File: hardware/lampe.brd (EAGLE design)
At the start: 63.2 x 62.2 mm, 45 parts, among them IC1 LM393N, IC2 ATMEGA168-20P, IC3 DS1307, Q1 IRFU9024N, Q2 16MHz, Q3 32.768kHz, T1 BC457B, T2 BC557B, T3 BC457B

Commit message: Cleanup
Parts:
- removed C2: 100nF, rcl:C025-025X050
- removed C3: 100uF, rcl:E2,5-6E
- removed C4: 22pF, rcl:C025-025X050
- removed C5: 100nF, rcl:C050-025X075
- removed D1: 1N4148, diode:D-2.5
- removed D2: 1N4148, diode:DO35-10
- removed D3: SB140, diode:ZDIO-2.5
- removed IC2: ATMEGA168-20P, adafruit:DIL28-3
- removed JP2: SUPPLY, pinhead:1X02
- removed JP3: (no value), pinhead:1X04
- removed L1: 100uH, rcl:6000-XXXX-RC
- removed Q1: IRFU9024N, transistor-power:I-PAK_TO251AA
- removed R1, R5: 10k, rcl:0204/5
- removed R10, R3: 4.7k, rcl:0204V
- removed R14: 10k, rcl:0204V
- removed R15: 15k, rcl:0207/10
- removed R2: 10k, rcl:RTRIM64W
- removed R22, R8: 1R*, rcl:0204/7
- removed R23: 4.7k, rcl:0204/7
- removed R4: 1k, rcl:0204/5
- removed R6: 10k, rcl:0207/10
- removed R7: 10R, rcl:0204/5
- removed R9: 1k, rcl:0207/10
- removed T1: BC457B, transistor:TO92-EBC
- removed T2: BC557B, transistor:TO92-EBC
- added ISP1: AVRISP-6, adafruit:AVRISP
- added KK1: PF750, heatsink:PF752
- added Q4: BUZ11BV, transistor-power:TO220BV
- added R24: 10, rcl:0204/7
- added R25, R30: 1W, rcl:0411/12
- added R26: 560, rcl:0204/7
- added R27: 10k, rcl:0207/10
- added R28: 10k, rcl:0204/5
- added R29: 1k, rcl:0204V
- added T4: BC547B, transistor-neu-to92:TO92-EBC
- added X1, X2: MKDSN1,5/2-5,08, con-phoenix-508:MKDSN1,5/2-5,08
- C1: value 1uF -> 100nF; device rcl:E2,5-6E -> rcl:C050-025X075
- C10: value 10uF -> 100pF; device rcl:E2,5-6E -> rcl:C025-025X050
- IC1: value LM393N -> ATMEGA168-20P; device linear:DIL08 -> adafruit:DIL28-3
- JP1: value LED -> GPIO; device pinhead:1X02 -> pinhead:1X05
- Q2: value 16MHz -> 16Mhz; device crystal:HC49/S -> adafruit:HC18U-V
- R11: device rcl:0204V -> rcl:0207/10
- T3: value BC457B -> BC547B; device transistor:TO92-EBC -> transistor-neu-to92:TO92-EBC
- moved JP1 47.1 mm to (40.6, 31.8), turned to 90 degrees
- moved IC1 33.2 mm to (49.5, 45.7), turned to 270 degrees
- moved C1 27.9 mm to (63.5, 49.5), turned to 180 degrees
- moved G1 17.8 mm to (81.3, 67.3), turned to 270 degrees
- moved C8 17.6 mm to (55.9, 45.7), turned to 90 degrees
- moved IC3 13.5 mm to (64.8, 63.5)
- moved Q3 13.5 mm to (67.3, 69.8)
- moved Q2 11.7 mm to (35.6, 41.9)
- moved R13 10.2 mm to (55.9, 63.5)
- moved C6 10.2 mm to (43.2, 41.9)
- moved R12 10.2 mm to (58.4, 62.2)
- moved C9 8.52 mm to (41.9, 47.0), turned to 180 degrees
- moved C7 8.13 mm to (40.6, 43.2), turned to 90 degrees
- moved C10 7.73 mm to (64.8, 36.8)
- moved T3 6.35 mm to (63.5, 40.6), turned to 0 degrees
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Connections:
- removed net N$10: IC1.7, R10.2, T1.B, T2.B
- removed net N$11: R7.1, T1.E, T2.E
- removed net N$15: D3.C, L1.2, Q1.2
- removed net N$16: Q1.1, R7.2
- removed net N$17: JP1.1, L1.1
- removed net N$20: IC2.1, R11.2
- removed net N$25: IC2.17, R15.2
- removed net N$26: C10.+, R14.1, R15.1, T3.B
- removed net N$27: IC2.5, JP3.2
- removed net N$28: IC2.6, JP3.3
- removed net N$30: C7.1, IC2.9, Q2.2
- new net N$37: Q4.G, R24.2
- new net N$38: Q4.D, X2.2
- new net N$39: Q4.S, R25.2, R26.1, R30.2
- new net N$40: C10.1, R26.2, T3.B
- new net N$41: C1.1, C10.2, R27.2, R28.2, T3.C, T4.B
- new net N$43: R24.1, R29.2, T4.E
- net +5V: now also IC1.20, IC1.21, IC1.7, ISP1.2, T4.C, X1.2, X2.1; no longer C2.1, C3.+, C5.1, IC1.8, IC2.20, IC2.21, IC2.7, JP2.2, Q1.3, R10.1, R23.1, R3.1, R5.1, T1.C
- net GND: now also C1.2, IC1.22, IC1.8, ISP1.6, JP1.1, R25.1, R28.1, R29.1, R30.1, X1.1; no longer C1.-, C10.-, C2.2, C3.-, C4.2, C5.2, D1.C, D3.A, IC1.4, IC2.22, IC2.8, JP2.1, JP3.4, R14.2, R22.2, R4.2, R6.2, R8.2, T2.C
- net N$1: now also IC1.15, R27.1; no longer D1.A, R1.1, R3.2
- net N$12: now also C7.1, IC1.9, Q2.2; no longer IC2.3, U$1.RXD
- net N$18: now also IC1.10; no longer IC2.10
- net N$19: now also IC1.28; no longer IC2.28
- net N$2: now also IC1.18, ISP1.1; no longer R1.2, R2.3
- net N$21: now also IC1.27; no longer IC2.27
- net N$23: now also IC1.3; no longer IC2.2
- net N$24: now also IC1.2, U$1.RXD; no longer IC2.4, JP3.1
- net N$3: now also IC1.19, ISP1.3; no longer C1.+, IC1.2, R2.2
- net N$4: now also IC1.1, ISP1.5, R11.2; no longer R2.1, R4.1
- net N$5: now also IC1.17, ISP1.4; no longer JP1.2, R22.1, R8.1, R9.2
- net N$6: now also IC1.12, JP1.4; no longer C4.1, IC1.3, R9.1
- net N$7: now also IC1.11, JP1.5; no longer D2.C, IC1.1
- net N$8: now also IC1.13, JP1.3; no longer D2.A, IC1.5, R23.2
- net N$9: now also IC1.14, JP1.2; no longer IC1.6, R5.2, R6.1, T3.C
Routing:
- net +5V: track 229.9 -> 140.2 mm
- net N$4: track 2.54 -> 43.2 mm
- net GND: track 336.6 -> 298.5 mm
- net N$9: track 40.6 -> 5.08 mm, vias 2 -> 0
- net N$10: track 27.9 -> 0.00 mm
- net N$39: track 0.00 -> 26.7 mm
- net N$37: track 0.00 -> 25.4 mm
- net N$41: track 0.00 -> 25.4 mm
- net N$5: track 7.62 -> 31.8 mm, vias 0 -> 2
- net N$38: track 0.00 -> 22.8 mm
- net N$2: track 5.08 -> 25.4 mm
- net N$30: track 15.5 -> 0.00 mm
- net N$26: track 15.2 -> 0.00 mm
- net N$11: track 15.2 -> 0.00 mm
- net N$21: track 20.3 -> 7.62 mm
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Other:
- board size 63.2 x 62.2 mm -> 68.2 x 68.6 mm
- board text added: "Lampe rev. 1"

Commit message: Minors.
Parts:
- added R1: 1k, rcl:0204V
- added R2: 10k, ptc-ntc:B57164
- R27: value 10k -> 6.1k
- R28: value 10k -> 1k
- R29: value 1k -> 10k
- moved ISP1 2.54 mm to (50.8, 22.9)
- moved R27 2.54 mm to (61.0, 29.2)
- moved U$1 2.54 mm to (38.1, 55.9)
- moved X1 2.54 mm to (73.7, 21.6)
- moved X2 2.54 mm to (83.8, 21.6)
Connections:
- new net N$10: IC1.23, R1.1, R2.1
- net +5V: now also R2.2
- net GND: now also R1.2
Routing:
- net +5V: track 140.2 -> 147.8 mm
- net GND: track 298.5 -> 306.1 mm
- net N$10: track 0.00 -> 5.08 mm
- net N$3: track 15.2 -> 17.8 mm
- net N$2: track 25.4 -> 27.9 mm
- net N$41: track 25.4 -> 27.9 mm
- net N$4: track 43.2 -> 45.7 mm
- net N$24: track 5.08 -> 7.62 mm
- net N$23: track 5.08 -> 7.62 mm
- net N$1: track 5.08 -> 2.54 mm
- net N$5: track 31.8 -> 34.3 mm
- net N$38: track 22.8 -> 25.4 mm
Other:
- board text added: "G"
- board text added: "R"
- board text added: "T"
- board text added: "V"

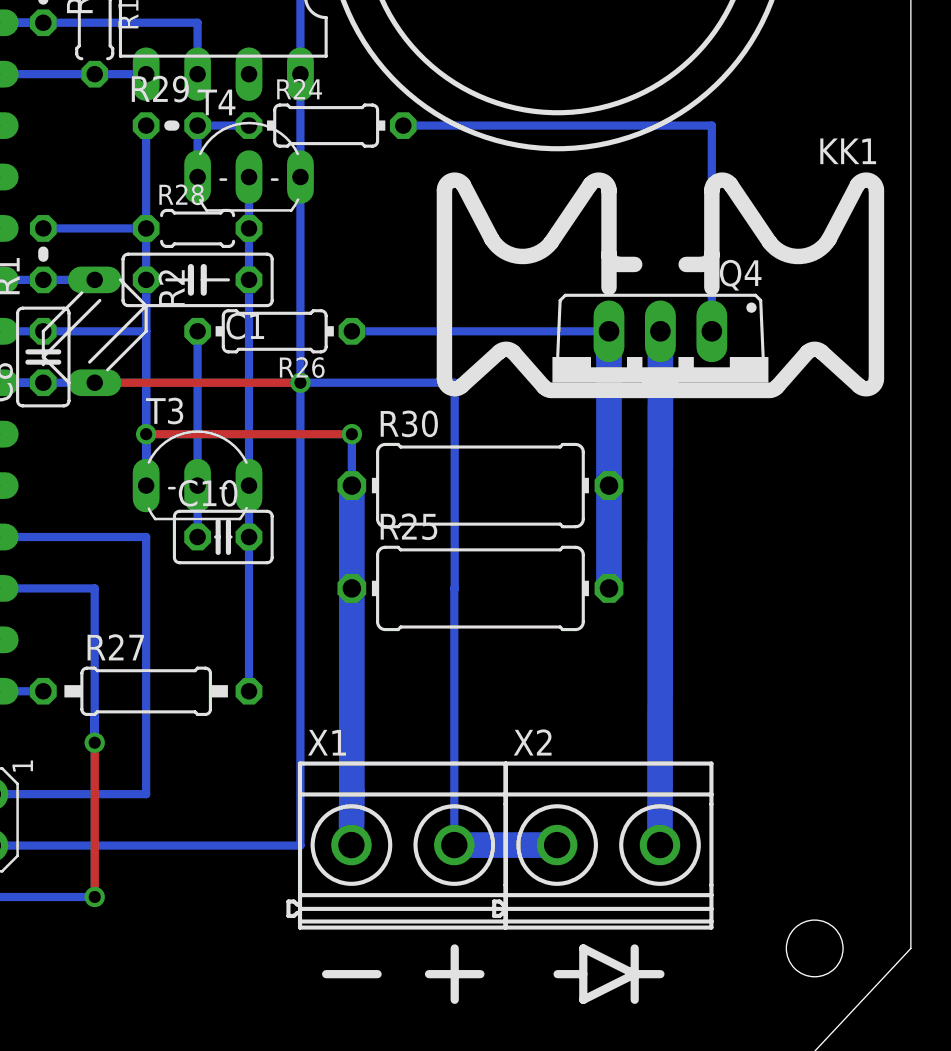
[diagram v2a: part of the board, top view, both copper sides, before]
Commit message: Fixed current reg.
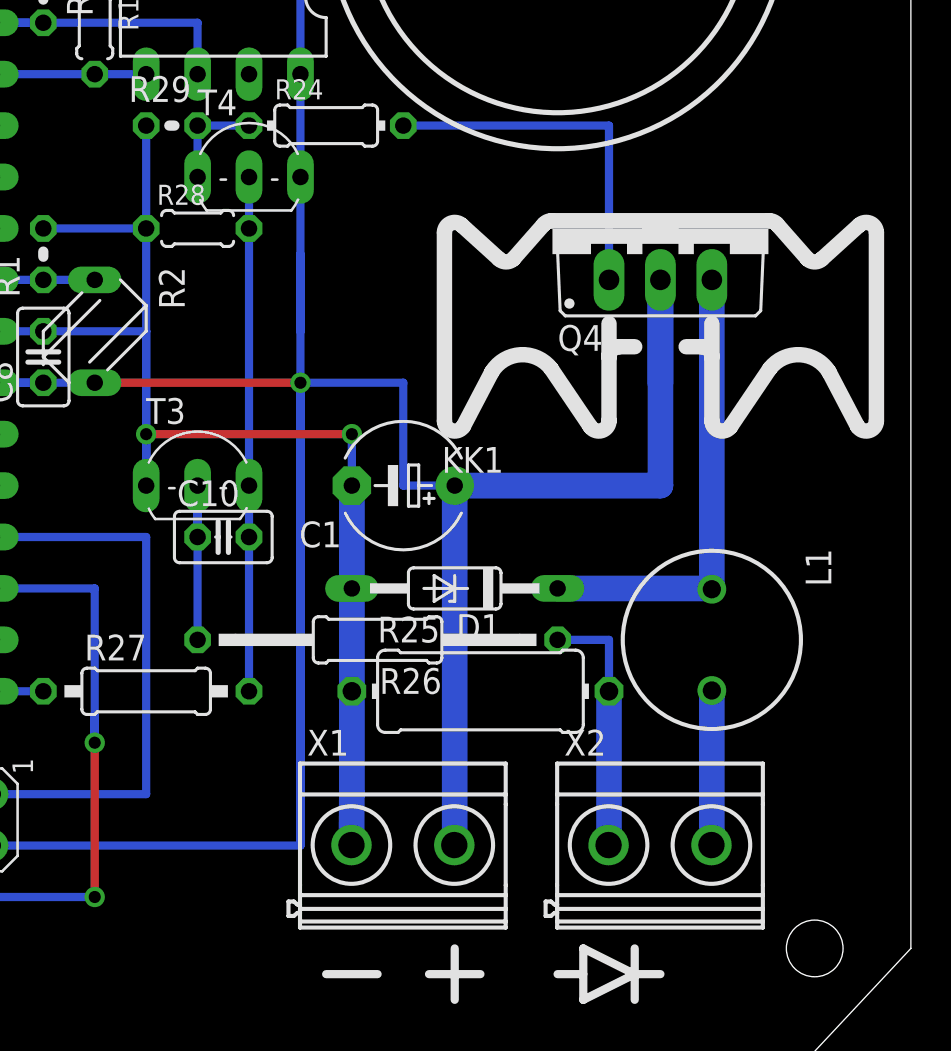
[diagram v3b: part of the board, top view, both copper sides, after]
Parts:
- removed R30: 1W, rcl:0411/12
- added D1: SB140, diode:DO35Z10
- added L1: 100uH, rcl:6000-XXXX-RC
- C1: value 100nF -> 100uF/35V; device rcl:C050-025X075 -> rcl:E5-6
- R26: device rcl:0204/7 -> rcl:0207/17
- R27: value 6.1k -> 4.7k
- moved R26 16.1 mm to (72.4, 31.8)
- moved C1 14.4 mm to (73.7, 39.4)
- moved KK1 7.62 mm to (86.4, 52.1), turned to 0 degrees
- moved Q4 7.62 mm to (86.4, 52.1), turned to 0 degrees
- moved R25 5.08 mm to (77.5, 29.2)
- moved X2 2.54 mm to (86.4, 21.6)
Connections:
- removed net N$38: Q4.D, X2.2
- new net N$11: D1.C, L1.1, Q4.S
- new net N$15: L1.2, X2.2
- net +5V: now also C1.+, Q4.D; no longer X2.1
- net GND: now also C1.-, D1.A; no longer C1.2, R30.1
- net N$39: now also X2.1; no longer Q4.S, R30.2
- net N$41: no longer C1.1
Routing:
- net +5V: track 147.8 -> 198.6 mm
- net N$38: track 25.4 -> 0.00 mm
- net N$11: track 0.00 -> 22.9 mm
- net N$39: track 26.7 -> 12.7 mm
- net N$15: track 0.00 -> 7.66 mm
- net N$37: track 25.4 -> 17.8 mm
- net GND: track 306.1 -> 303.6 mm
- net N$41: track 27.9 -> 25.4 mm

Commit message: Updated circuit and board PDFs.
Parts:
- moved T4 5.08 mm to (66.0, 50.8)
- moved R24 5.08 mm to (69.8, 52.1)
- moved R28 5.08 mm to (63.5, 47.0)
- moved R29 5.08 mm to (62.2, 52.1)
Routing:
- net GND: track 303.6 -> 223.5 mm
- net +5V: track 198.6 -> 165.5 mm
- net N$41: track 25.4 -> 20.3 mm
- net N$37: track 17.8 -> 12.7 mm
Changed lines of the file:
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@@
 <?xml version="1.0" encoding="utf-8"?>
 <!DOCTYPE eagle SYSTEM "eagle.dtd">
-<eagle version="7.1.0">
+<eagle version="7.2.0">
 <drawing>
 <settings>
@@
 <element name="R13" library="rcl" package="0204V" value="10k" x="55.88" y="63.5" rot="R270"/>
 <element name="U$1" library="jy-mcu" package="JY-MCU" value="JY-MCU" x="38.1" y="55.88" rot="R180"/>
-<element name="R24" library="rcl" package="0204/7" value="10" x="69.85" y="57.15"/>
+<element name="R24" library="rcl" package="0204/7" value="10" x="69.85" y="52.07"/>
 <element name="Q4" library="transistor-power" package="TO220BV" value="BUZ11BV" x="86.36" y="52.07"/>
 <element name="R25" library="rcl" package="0411/12" value="1W" x="77.47" y="29.21"/>
@@
 <element name="C10" library="rcl" package="C025-025X050" value="100pF" x="64.77" y="36.83"/>
 <element name="R27" library="rcl" package="0207/10" value="4.7k" x="60.96" y="29.21"/>
-<element name="R28" library="rcl" package="0204/5" value="1k" x="63.5" y="52.07"/>
-<element name="T4" library="transistor-neu-to92" package="TO92-EBC" value="BC547B" x="66.04" y="55.88"/>
-<element name="R29" library="rcl" package="0204V" value="10k" x="62.23" y="57.15"/>
+<element name="R28" library="rcl" package="0204/5" value="1k" x="63.5" y="46.99"/>
+<element name="T4" library="transistor-neu-to92" package="TO92-EBC" value="BC547B" x="66.04" y="50.8"/>
+<element name="R29" library="rcl" package="0204V" value="10k" x="62.23" y="52.07"/>
 <element name="X1" library="con-phoenix-508" package="MKDSN1,5/2-5,08" value="MKDSN1,5/2-5,08" x="73.66" y="21.59"/>
 <element name="X2" library="con-phoenix-508" package="MKDSN1,5/2-5,08" value="MKDSN1,5/2-5,08" x="86.36" y="21.59"/>
@@
 <contactref element="R12" pad="1"/>
 <wire x1="68.58" y1="59.69" x2="68.58" y2="64.77" width="0.4064" layer="16"/>
-<wire x1="59.69" y1="64.77" x2="58.42" y2="64.77" width="0.4064" layer="16"/>
 <contactref element="C9" pad="1"/>
 <contactref element="U$1" pad="VCC"/>
 <contactref element="T4" pad="C"/>
-<wire x1="68.58" y1="54.61" x2="68.58" y2="59.69" width="0.4064" layer="16"/>
+<wire x1="68.58" y1="49.53" x2="68.58" y2="59.69" width="0.4064" layer="16"/>
 <wire x1="38.1" y1="52.07" x2="43.18" y2="52.07" width="0.4064" layer="16"/>
-<wire x1="68.58" y1="64.77" x2="59.69" y2="64.77" width="0.4064" layer="16"/>
-<wire x1="68.58" y1="54.61" x2="68.58" y2="46.99" width="0.4064" layer="16"/>
+<wire x1="68.58" y1="64.77" x2="58.42" y2="64.77" width="0.4064" layer="16"/>
 <contactref element="ISP1" pad="2"/>
 <contactref element="IC1" pad="7"/>
@@
 <contactref element="X1" pad="2"/>
 <wire x1="53.34" y1="21.59" x2="68.58" y2="21.59" width="0.4064" layer="16"/>
-<wire x1="68.58" y1="21.59" x2="68.58" y2="44.45" width="0.4064" layer="16"/>
 <via x="68.58" y="44.45" extent="1-16" drill="0.6" shape="square"/>
 <wire x1="68.58" y1="44.45" x2="58.42" y2="44.45" width="0.4064" layer="1"/>
 <via x="58.42" y="44.45" extent="1-16" drill="0.6" shape="square"/>
 <wire x1="58.42" y1="44.45" x2="55.88" y2="44.45" width="0.4064" layer="16"/>
-<wire x1="55.88" y1="44.45" x2="53.34" y2="44.45" width="0.4064" layer="16"/>
 <wire x1="45.72" y1="46.99" x2="43.18" y2="46.99" width="0.4064" layer="16"/>
 <wire x1="43.18" y1="46.99" x2="43.18" y2="52.07" width="0.4064" layer="16"/>
@@
 <contactref element="Q4" pad="D"/>
 <contactref element="C1" pad="+"/>
-<wire x1="76.1789" y1="21.615" x2="76.2" y2="21.615" width="1.27" layer="16"/>
-<wire x1="76.2" y1="21.615" x2="76.2" y2="39.3489" width="1.27" layer="16"/>
+<wire x1="76.2" y1="21.615" x2="76.2" y2="39.37" width="1.27" layer="16"/>
 <wire x1="76.1789" y1="21.615" x2="76.2" y2="21.615" width="1.27" layer="16"/>
 <wire x1="86.36" y1="49.53" x2="86.36" y2="44.45" width="1.27" layer="16"/>
-<wire x1="68.58" y1="44.45" x2="68.58" y2="46.99" width="0.4064" layer="16"/>
-<wire x1="68.58" y1="46.99" x2="68.58" y2="50.8" width="0.4064" layer="16"/>
-<wire x1="68.58" y1="50.8" x2="68.58" y2="46.99" width="0.4064" layer="16"/>
-<wire x1="76.2" y1="39.37" x2="76.2" y2="39.3489" width="1.27" layer="16"/>
-<wire x1="76.2" y1="39.3489" x2="76.2" y2="39.37" width="1.27" layer="16"/>
-<wire x1="76.2" y1="39.3489" x2="76.2" y2="39.37" width="1.27" layer="16"/>
+<wire x1="68.58" y1="49.53" x2="68.58" y2="44.45" width="0.4064" layer="16"/>
 <wire x1="86.36" y1="49.53" x2="86.36" y2="39.37" width="1.27" layer="16"/>
 <wire x1="86.36" y1="39.37" x2="76.2" y2="39.37" width="1.27" layer="16"/>
@@
 <contactref element="R28" pad="1"/>
 <contactref element="R29" pad="1"/>
-<wire x1="60.96" y1="39.37" x2="60.96" y2="40.64" width="0.4064" layer="16"/>
-<wire x1="60.96" y1="40.64" x2="60.96" y2="41.91" width="0.4064" layer="16"/>
-<wire x1="60.96" y1="41.91" x2="60.96" y2="46.99" width="0.4064" layer="16"/>
 <wire x1="71.12" y1="34.29" x2="71.12" y2="29.21" width="1.27" layer="16"/>
 <wire x1="71.12" y1="29.21" x2="71.12" y2="24.155" width="1.27" layer="16"/>
@@
 <contactref element="IC1" pad="8"/>
 <contactref element="IC1" pad="22"/>
-<wire x1="71.12" y1="24.155" x2="71.12" y2="24.13" width="1.27" layer="16"/>
-<wire x1="53.34" y1="46.99" x2="50.8" y2="46.99" width="0.4064" layer="16"/>
-<wire x1="81.28" y1="74.93" x2="60.96" y2="74.93" width="0.4064" layer="16"/>
-<wire x1="60.96" y1="74.93" x2="60.96" y2="67.31" width="0.4064" layer="16"/>
 <contactref element="X1" pad="1"/>
-<wire x1="60.96" y1="39.37" x2="60.96" y2="40.64" width="0.4064" layer="16"/>
-<wire x1="60.96" y1="40.64" x2="60.96" y2="41.91" width="0.4064" layer="16"/>
 <wire x1="60.96" y1="41.91" x2="60.96" y2="46.99" width="0.4064" layer="16"/>
 <wire x1="71.0989" y1="21.615" x2="71.12" y2="24.155" width="1.27" layer="16"/>
@@
 <wire x1="60.96" y1="41.91" x2="71.12" y2="41.91" width="0.4064" layer="1"/>
 <via x="71.12" y="41.91" extent="1-16" drill="0.6" shape="square"/>
-<wire x1="60.96" y1="57.15" x2="60.96" y2="52.07" width="0.4064" layer="16"/>
+<wire x1="60.96" y1="52.07" x2="60.96" y2="46.99" width="0.4064" layer="16"/>
 <wire x1="53.34" y1="46.99" x2="50.8" y2="46.99" width="0.4064" layer="16"/>
 <contactref element="JP1" pad="1"/>
-<wire x1="40.64" y1="26.67" x2="40.64" y2="21.59" width="0.4064" layer="16"/>
-<wire x1="40.64" y1="21.59" x2="48.26" y2="21.59" width="0.4064" layer="16"/>
-<wire x1="60.96" y1="67.31" x2="60.96" y2="74.93" width="0.4064" layer="16"/>
-<wire x1="60.96" y1="41.91" x2="60.96" y2="40.64" width="0.4064" layer="16"/>
+<wire x1="60.96" y1="41.91" x2="60.96" y2="39.37" width="0.4064" layer="16"/>
 <wire x1="45.72" y1="44.45" x2="43.18" y2="44.45" width="0.4064" layer="16"/>
 <wire x1="40.64" y1="44.45" x2="43.18" y2="44.45" width="0.4064" layer="16"/>
-<wire x1="45.72" y1="44.45" x2="38.1" y2="44.45" width="0.4064" layer="16"/>
-<wire x1="38.1" y1="44.45" x2="38.1" y2="46.99" width="0.4064" layer="16"/>
 <wire x1="40.64" y1="46.99" x2="38.1" y2="46.99" width="0.4064" layer="16"/>
 <wire x1="45.72" y1="44.45" x2="38.1" y2="44.45" width="0.4064" layer="16"/>
@@
 <wire x1="55.88" y1="46.99" x2="60.96" y2="46.99" width="0.4064" layer="16"/>
 <wire x1="50.8" y1="46.99" x2="50.8" y2="67.31" width="0.4064" layer="16"/>
-<wire x1="50.8" y1="67.31" x2="38.1" y2="67.31" width="0.4064" layer="16"/>
+<wire x1="50.8" y1="67.31" x2="33.02" y2="67.31" width="0.4064" layer="16"/>
 <wire x1="81.28" y1="74.93" x2="60.96" y2="74.93" width="0.4064" layer="16"/>
 <wire x1="60.96" y1="74.93" x2="60.96" y2="67.31" width="0.4064" layer="16"/>
@@
 <wire x1="40.64" y1="26.67" x2="33.02" y2="26.67" width="0.4064" layer="16"/>
 <wire x1="33.02" y1="26.67" x2="33.02" y2="46.99" width="0.4064" layer="16"/>
-<wire x1="33.02" y1="46.99" x2="38.1" y2="46.99" width="0.4064" layer="16"/>
 <wire x1="38.1" y1="46.99" x2="33.02" y2="46.99" width="0.4064" layer="16"/>
 <wire x1="33.02" y1="46.99" x2="33.02" y2="54.61" width="0.4064" layer="16"/>
 <wire x1="33.02" y1="54.61" x2="33.02" y2="67.31" width="0.4064" layer="16"/>
-<wire x1="33.02" y1="67.31" x2="38.1" y2="67.31" width="0.4064" layer="16"/>
 <wire x1="38.1" y1="54.61" x2="33.02" y2="54.61" width="0.4064" layer="16"/>
 <contactref element="R1" pad="2"/>
-<wire x1="55.88" y1="52.07" x2="60.96" y2="52.07" width="0.4064" layer="16"/>
 <contactref element="C1" pad="-"/>
 <contactref element="D1" pad="A"/>
-<wire x1="60.96" y1="52.07" x2="60.96" y2="46.99" width="0.4064" layer="16"/>
 <wire x1="71.12" y1="34.29" x2="71.12" y2="39.37" width="1.27" layer="16"/>
 <wire x1="71.12" y1="39.37" x2="71.12" y2="41.91" width="0.4064" layer="16"/>
+<wire x1="55.88" y1="52.07" x2="60.96" y2="52.07" width="0.4064" layer="16"/>
 </signal>
 <signal name="N$13">
@@
 <contactref element="Q4" pad="G"/>
 <contactref element="R24" pad="2"/>
-<wire x1="83.82" y1="57.15" x2="73.66" y2="57.15" width="0.4064" layer="16"/>
-<wire x1="83.82" y1="49.53" x2="83.82" y2="57.15" width="0.4064" layer="16"/>
+<wire x1="83.82" y1="52.07" x2="73.66" y2="52.07" width="0.4064" layer="16"/>
+<wire x1="83.82" y1="49.53" x2="83.82" y2="52.07" width="0.4064" layer="16"/>
 </signal>
 <signal name="N$39">
@@
 <contactref element="R28" pad="2"/>
 <contactref element="R27" pad="2"/>
-<wire x1="66.04" y1="54.61" x2="66.04" y2="52.07" width="0.4064" layer="16"/>
+<wire x1="66.04" y1="49.53" x2="66.04" y2="46.99" width="0.4064" layer="16"/>
 <wire x1="66.04" y1="29.21" x2="66.04" y2="36.83" width="0.4064" layer="16"/>
 <wire x1="66.04" y1="39.37" x2="66.04" y2="36.83" width="0.4064" layer="16"/>
-<wire x1="66.04" y1="52.07" x2="66.04" y2="39.37" width="0.4064" layer="16"/>
+<wire x1="66.04" y1="46.99" x2="66.04" y2="39.37" width="0.4064" layer="16"/>
 </signal>
 <signal name="N$43">
@@
 <contactref element="R29" pad="2"/>
 <contactref element="T4" pad="E"/>
-<wire x1="63.5" y1="54.61" x2="63.5" y2="57.15" width="0.4064" layer="16"/>
-<wire x1="63.5" y1="57.15" x2="66.04" y2="57.15" width="0.4064" layer="16"/>
+<wire x1="63.5" y1="49.53" x2="63.5" y2="52.07" width="0.4064" layer="16"/>
+<wire x1="63.5" y1="52.07" x2="66.04" y2="52.07" width="0.4064" layer="16"/>
 </signal>
 <signal name="N$2">
